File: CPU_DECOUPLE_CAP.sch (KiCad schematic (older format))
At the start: 12 parts

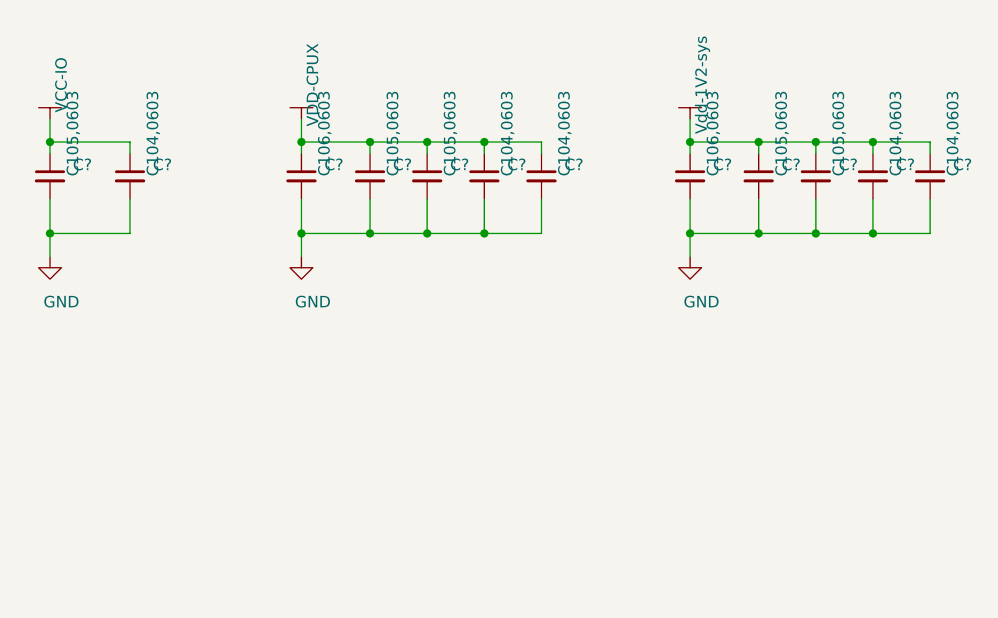
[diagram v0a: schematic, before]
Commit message: update decouple capacitor,
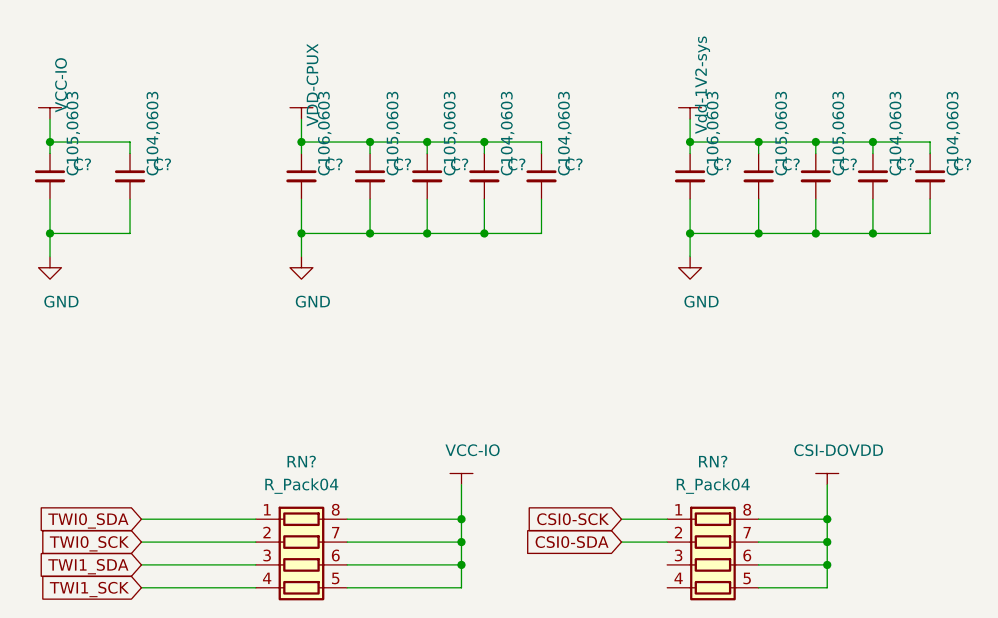
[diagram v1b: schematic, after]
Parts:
- added RN? (x2): R_Pack04, symbol Device:R_Pack04
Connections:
- net VCC-IO: now also RN?.5 (R4.2), RN?.6 (R3.2), RN?.7 (R2.2), RN?.8 (R1.2)
- new net CSI-DOVDD: RN?.5 (R4.2), RN?.6 (R3.2), RN?.7 (R2.2), RN?.8 (R1.2)
- new net CSI0-SCK: RN?.1 (R1.1)
- new net CSI0-SDA: RN?.2 (R2.1)
- new net TWI0_SCK: RN?.2 (R2.1)
- new net TWI0_SDA: RN?.1 (R1.1)
- new net TWI1_SCK: RN?.4 (R4.1)
- new net TWI1_SDA: RN?.3 (R3.1)
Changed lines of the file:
@@
 	1    0    0    -1
 $EndComp
+$Comp
+L taobao-components:VCC-IO #PWR?
+U 1 1 5C34E9EA
+P 8750 4500
+F 0 "#PWR?" H 8750 4350 50  0001 C CNN
+F 1 "VCC-IO" H 8800 4650 50  0000 C CNN
+F 2 "" H 8750 4500 50  0001 C CNN
+F 3 "" H 8750 4500 50  0001 C CNN
+	1    8750 4500
+	1    0    0    -1
+$EndComp
+$Comp
+L Device:R_Pack04 RN?
+U 1 1 5C34EDE5
+P 8050 4850
+F 0 "RN?" V 7600 4850 50  0000 C CNN
+F 1 "R_Pack04" V 7700 4850 50  0000 C CNN
+F 2 "" V 8325 4850 50  0001 C CNN
+F 3 "~" H 8050 4850 50  0001 C CNN
+	1    8050 4850
+	0    1    1    0
+$EndComp
+Wire Wire Line
+	8750 4500 8750 4650
+Wire Wire Line
+	8750 4950 8250 4950
+Wire Wire Line
+	8250 4650 8750 4650
+Connection ~ 8750 4650
+Wire Wire Line
+	8750 4650 8750 4750
+Wire Wire Line
+	8250 4750 8750 4750
+Wire Wire Line
+	8250 4850 8750 4850
+Connection ~ 8750 4850
+Wire Wire Line
+	8750 4850 8750 4950
+Connection ~ 8750 4750
+Wire Wire Line
+	8750 4750 8750 4850
+Text GLabel 7350 4650 0    50   Input ~ 0
+TWI0_SDA
+Text GLabel 7350 4750 0    50   Input ~ 0
+TWI0_SCK
+Text GLabel 7350 4850 0    50   Input ~ 0
+TWI1_SDA
+Text GLabel 7350 4950 0    50   Input ~ 0
+TWI1_SCK
+Wire Wire Line
+	7350 4650 7850 4650
+Wire Wire Line
+	7350 4750 7850 4750
+Wire Wire Line
+	7350 4850 7850 4850
+Wire Wire Line
+	7350 4950 7850 4950
+$Comp
+L taobao-components:CSI-DOVDD #PWR?
+U 1 1 5C351AE4
+P 10350 4500
+F 0 "#PWR?" H 10350 4350 50  0001 C CNN
+F 1 "CSI-DOVDD" H 10400 4650 50  0000 C CNN
+F 2 "" H 10350 4500 50  0001 C CNN
+F 3 "" H 10350 4500 50  0001 C CNN
+	1    10350 4500
+	1    0    0    -1
+$EndComp
+$Comp
+L Device:R_Pack04 RN?
+U 1 1 5C351B38
+P 9850 4850
+F 0 "RN?" V 9400 4850 50  0000 C CNN
+F 1 "R_Pack04" V 9500 4850 50  0000 C CNN
+F 2 "" V 10125 4850 50  0001 C CNN
+F 3 "~" H 9850 4850 50  0001 C CNN
+	1    9850 4850
+	0    1    1    0
+$EndComp
+Wire Wire Line
+	10350 4500 10350 4650
+Wire Wire Line
+	10350 4650 10050 4650
+Wire Wire Line
+	10350 4750 10050 4750
+Wire Wire Line
+	10350 4850 10050 4850
+Wire Wire Line
+	10350 4950 10050 4950
+Wire Wire Line
+	10350 4950 10350 4850
+Connection ~ 10350 4650
+Connection ~ 10350 4750
+Wire Wire Line
+	10350 4750 10350 4650
+Connection ~ 10350 4850
+Wire Wire Line
+	10350 4850 10350 4750
+Text GLabel 9450 4650 0    50   Input ~ 0
+CSI0-SCK
+Wire Wire Line
+	9450 4650 9650 4650
+Text GLabel 9450 4750 0    50   Input ~ 0
+CSI0-SDA
+Wire Wire Line
+	9450 4750 9650 4750
 $EndSCHEMATC
